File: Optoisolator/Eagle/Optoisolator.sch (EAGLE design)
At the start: 18 parts

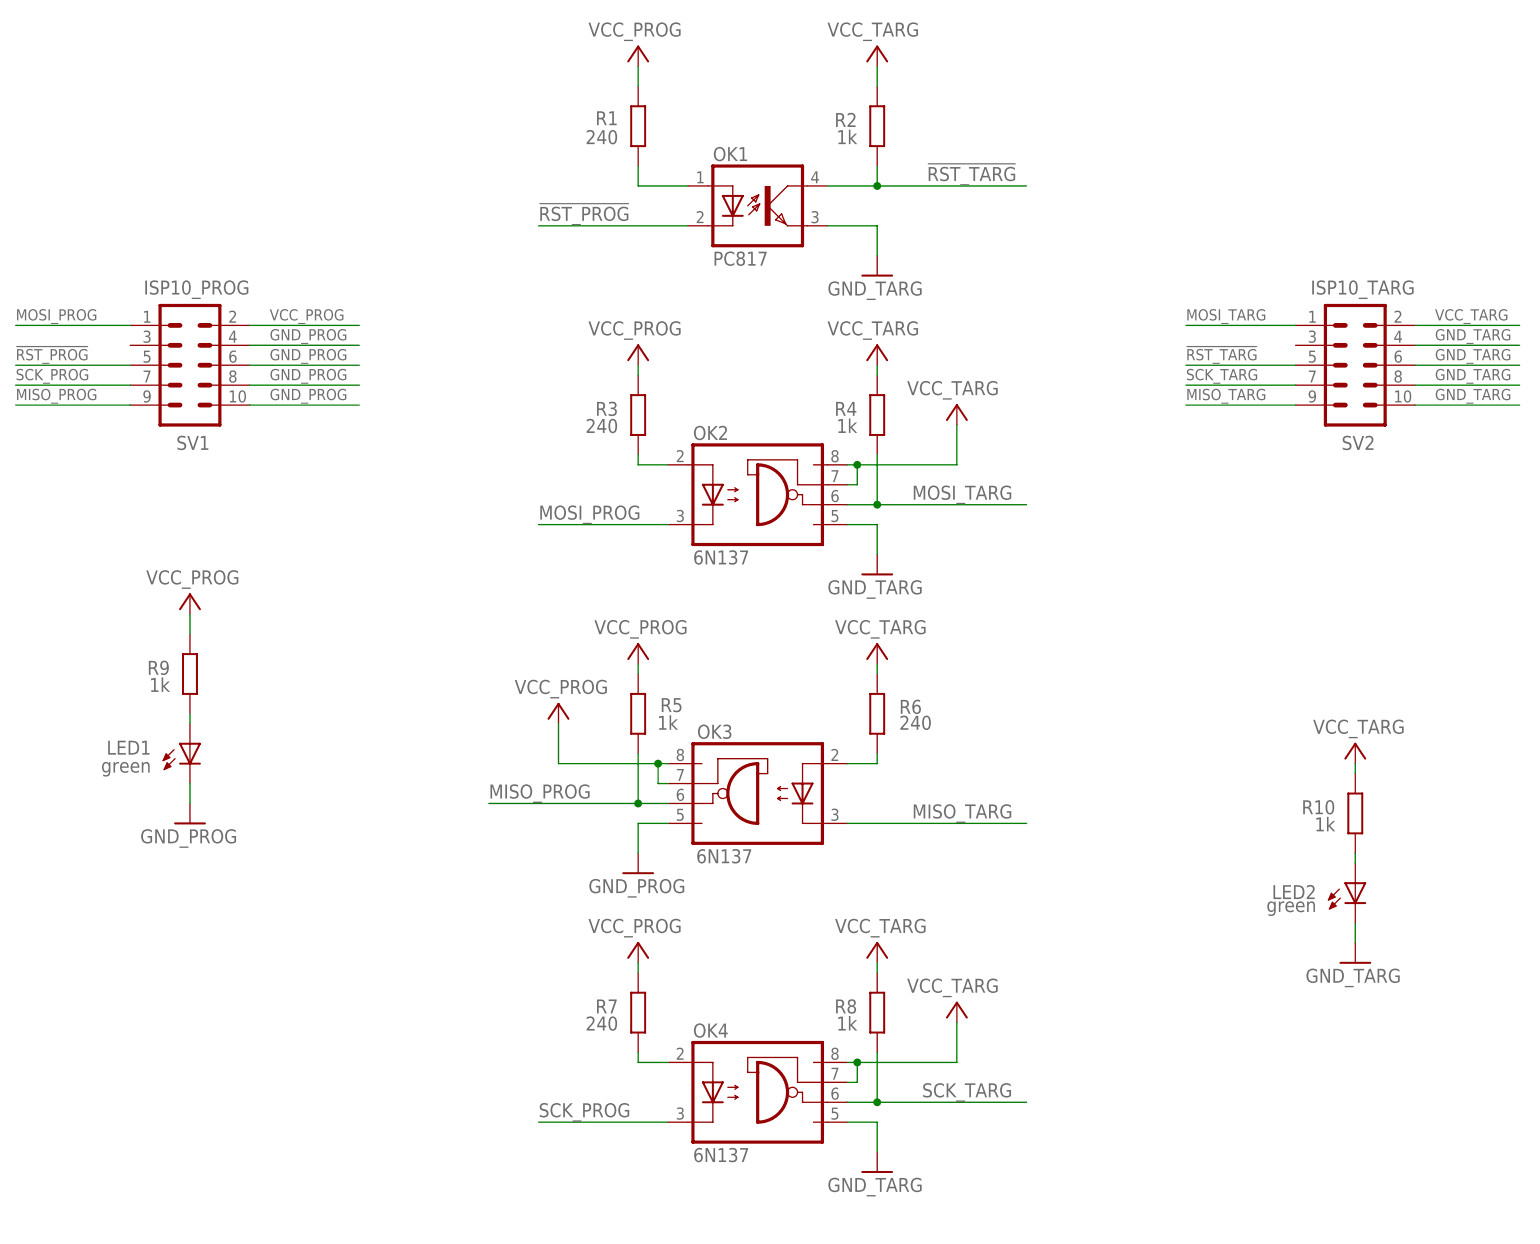
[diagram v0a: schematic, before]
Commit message: Routed right-hand side of optoisolator
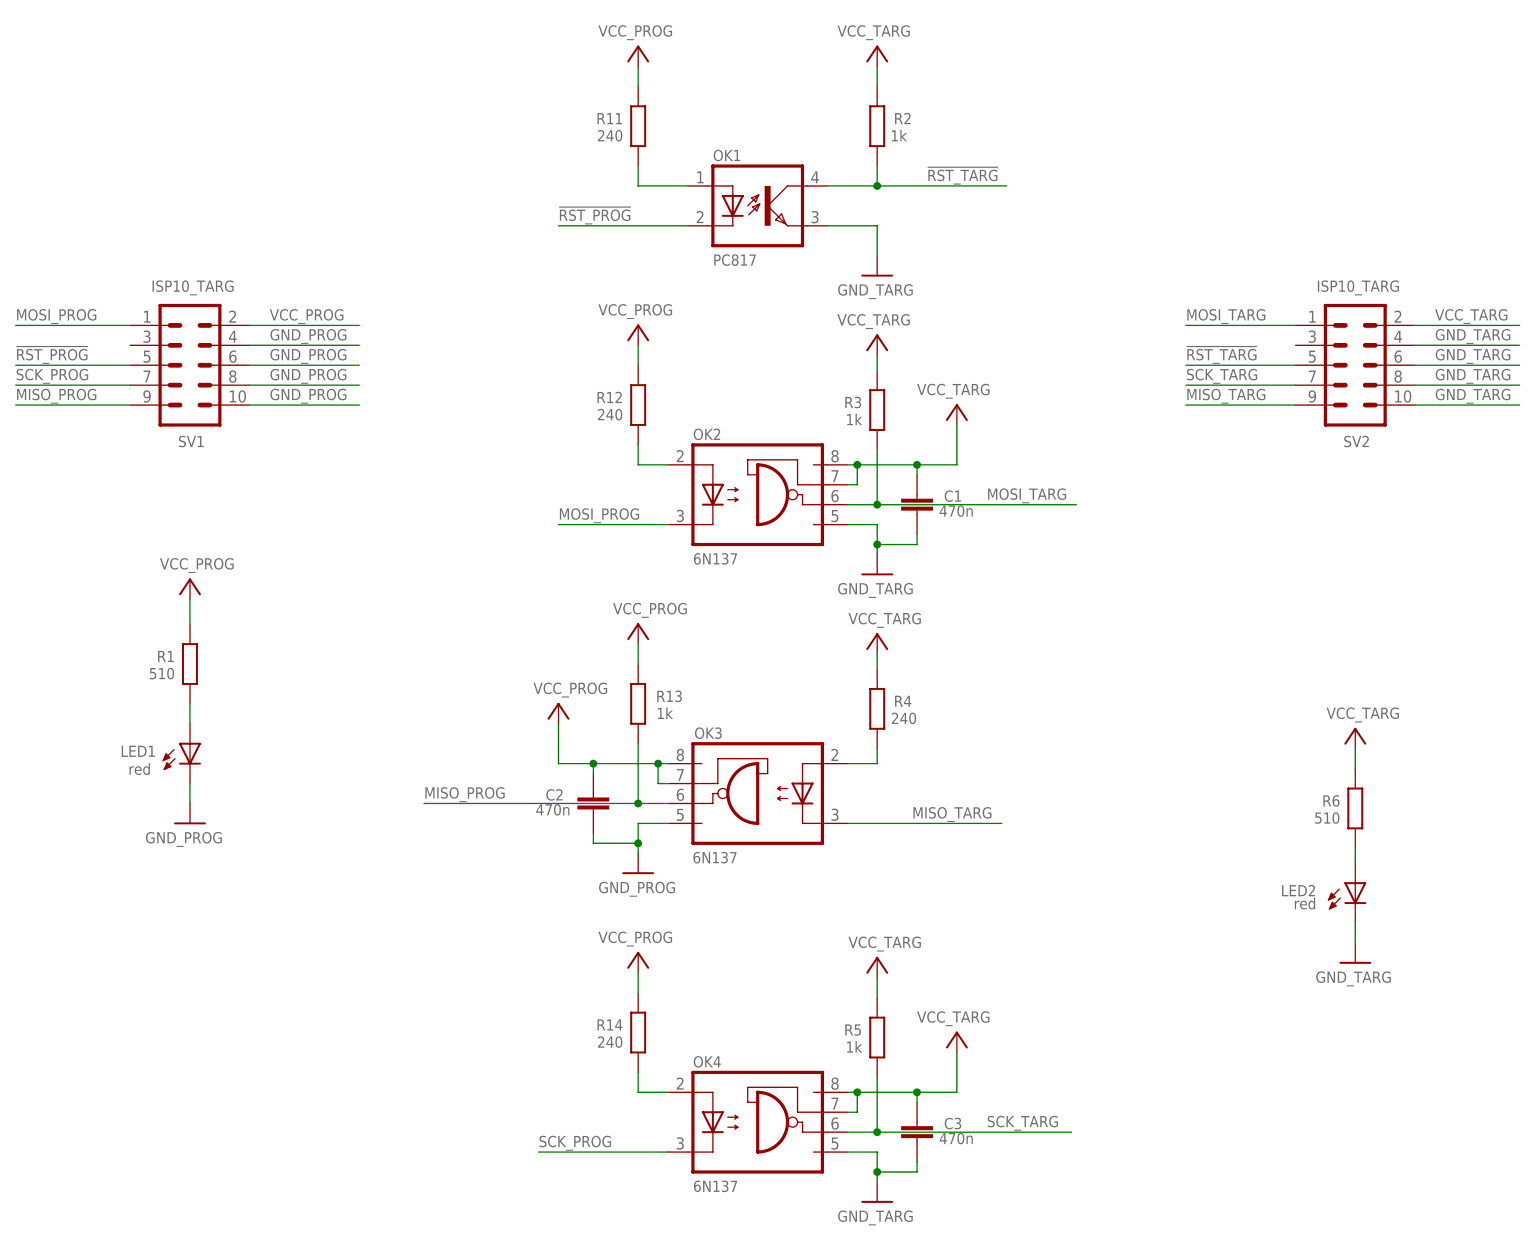
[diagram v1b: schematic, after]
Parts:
- removed R10, R8, R9: 1k, Analog:R-EU_0207/10
- removed R7: 240, Analog:R-EU_0207/10
- added C1, C2, C3: 470n, Optoisolator:C-EU050-025X075
- added R11, R12, R14: 240, Passive-PoE-ClassB:RESR1206
- added R13: 1k, Passive-PoE-ClassB:RESR1206
- LED1, LED2: value green -> red; device Passive.PoE.LV:LED3MM -> Optoisolator:LED3MM
- OK1: device optocoupler:PC817 -> Optoisolator:PC817
- OK2, OK3, OK4: device optocoupler:6N137 -> Optoisolator:6N137
- R1, R6: value 240 -> 510; device Analog:R-EU_0207/10 -> Passive-PoE-ClassB:RESR1206
- R2, R5: device Analog:R-EU_0207/10 -> Passive-PoE-ClassB:RESR1206
- R3: value 240 -> 1k; device Analog:R-EU_0207/10 -> Passive-PoE-ClassB:RESR1206
- R4: value 1k -> 240; device Analog:R-EU_0207/10 -> Passive-PoE-ClassB:RESR1206
- SV1: value ISP10_PROG -> ISP10_TARG; device con-ml:ML10L -> Optoisolator:ML10; OC_FARNELL (none) -> unknown; OC_NEWARK (none) -> unknown
- SV2: device con-ml:ML10 -> Optoisolator:ML10
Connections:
- net GND_PROG: now also C2.2
- net GND_TARG: now also C1.2, C3.2
- net MISO_PROG: now also R13.1; no longer R5.1
- net MOSI_TARG: now also R3.1; no longer R4.1
- net N$1: now also R11.1; no longer R1.1
- net N$12: now also R4.1; no longer R6.1
- net N$2: now also R12.1; no longer R3.1
- net N$3: now also R14.1; no longer R7.1
- net N$4: now also R6.1; no longer R10.1
- net N$5: now also R1.1; no longer R9.1
- net SCK_TARG: now also R5.1; no longer R8.1
- net VCC_PROG: now also C2.1, R11.2, R12.2, R13.2, R14.2; no longer R3.2, R5.2, R7.2, R9.2
- net VCC_TARG: now also C1.1, C3.1, R3.2, R5.2; no longer R10.2, R8.2
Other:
- moved on the sheet: OK4, R1, R3, R4, R5, R6

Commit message: Replaced through-hole bypass capacitors with smd one
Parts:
- C1, C2, C3: device Optoisolator:C-EU050-025X075 -> Passive-PoE-ClassB:CAPC1206
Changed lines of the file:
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@@
 <setting verticaltext="up"/>
 </settings>
-<grid distance="2.54" unitdist="mm" unit="mm" style="lines" multiple="1" display="yes" altdistance="0.01" altunitdist="inch" altunit="inch"/>
+<grid distance="0.1" unitdist="inch" unit="inch" style="lines" multiple="1" display="no" altdistance="0.01" altunitdist="inch" altunit="inch"/>
 <layers>
 <layer number="1" name="Top" color="4" fill="1" visible="no" active="no"/>
@@
 <part name="R5" library="Passive-PoE-ClassB" deviceset="RES" device="R1206" value="1k"/>
 <part name="R6" library="Passive-PoE-ClassB" deviceset="RES" device="R1206" value="510"/>
-<part name="C1" library="Optoisolator" deviceset="C-EU" device="050-025X075" value="470n"/>
-<part name="C2" library="Optoisolator" deviceset="C-EU" device="050-025X075" value="470n"/>
-<part name="C3" library="Optoisolator" deviceset="C-EU" device="050-025X075" value="470n"/>
+<part name="C1" library="Passive-PoE-ClassB" deviceset="CAP" device="C1206" value="470n"/>
+<part name="C2" library="Passive-PoE-ClassB" deviceset="CAP" device="C1206" value="470n"/>
+<part name="C3" library="Passive-PoE-ClassB" deviceset="CAP" device="C1206" value="470n"/>
 </parts>
 <sheets>
